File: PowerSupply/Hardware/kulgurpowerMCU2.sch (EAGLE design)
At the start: 80 parts, among them IC1 TPS77050, IC2 TPS77333DGK, X1 12Mhz, X6 C-GRID-10-70543, X7 C-GRID-10-70543, X8 C-GRID-10-70543, X9 C-GRID-10-70543

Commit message: Lot of changes to schematics. A lot.
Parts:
- removed AN3, BUZZER: TPB1,27, testpad:TPB1,27
- removed C51, C56: 0,1, SparkFun:CAP0603-CAP
- removed CN1: (no value), adafruit:USBMINIB
- removed D1, D3, D4, D5, D6: BAT54, diode:BAT54
- removed ERROR, HEARTBEAT: (no value), SparkFun:LED0603
- removed IC1: TPS77050, texas:TPS77050
- removed JP1: (no value), pinhead:PINHD-2X7
- removed R47, R52: 1k, SparkFun:RESISTOR0603-RES
- removed R50: 100k, SparkFun:RESISTOR0603-RES
- removed R51: 18k, SparkFun:RESISTOR0603-RES
- removed S3: (no value), switch-omron:10-XX
- removed S4, S5: SWITCH-MOMENTARY-212MM, SparkFun-Electromechanical:SWITCH-MOMENTARY-212MM
- removed SG2: BUZZERSMD3, SparkFun:BUZZERSMD3
- removed X6, X7, X8, X9: C-GRID-10-70543, con-molex:C-GRID-10-70543
- added AN0, EMLE, TP2, TP6, TP7: TPB1,27, testpad:TPB1,27
- added C12: 0.1, SparkFun:CAP0603-CAP
- added C14: 0,1, SparkFun:CAP0603-CAP
- added C16, C18, C41: (no value), rcl:CPOL-EUC/6032-28R
- added C19, C21, C24: 100n, rcl:C-EUC0603
- added C20, C25: 2.2nF / 50V, smd-ipc:C0402
- added C23: 1uF/ 26V, resistor:C-EUC0805
- added C27, C30, C31, C32, C33, C34, C35, C36, C37, C38, C39: 0.1, rcl:C-EUC0603
- added CN2: (no value), adafruit:USBMINIB
- added D7: BAT54, diode:BAT54
- added D8: LED-RGB-CC-THRUDIFFUSE, SparkFun-LED:LED-RGB-CC-THRUDIFFUSE
- added ERROR1, HEARTBEAT1, LED0, LED1, LED2, LED3, LED4, LED5, LED6, LED7: (no value), SparkFun:LED0603
- added IC3: REG1117-5, burr-brown:REG1117
- added JP2: (no value), pinhead:PINHD-2X7
- added L1: 4,7uH, wuerth-elektronik:WE-KIHQ_0805
- added L2, L4, L5: 4,7uH, inductors:DR73
- added R20, R21, R28, R29, R30, R31, R32, R33, R34: 1k, rcl:R-EU_R0603
- added R22: 47k, rcl:R-EU_R0603
- added R23: 100k, rcl:R-EU_R0603
- added R24, R25: 22r, rcl:R-EU_R0603
- added R26: 30k, rcl:R-EU_R0603
- added R27: 17k, rcl:R-EU_R0603
- added S6: SW1, SparkFun-Electromechanical:TAC_SWITCHSMD
- added S7: SW2, SparkFun-Electromechanical:TAC_SWITCHSMD
- added S8: SW3, SparkFun-Electromechanical:TAC_SWITCHSMD
- added S9: RESET, SparkFun-Electromechanical:SWITCH-MOMENTARY-2SIDE_EZ
- added SG1: BUZZERSMD3, SparkFun:BUZZERSMD3
- added SV2: (no value), con-lstb:MA13-2
- added TP10, TP15, TP5, TP8: TPB2,54, testpad:TPB2,54
- added TPLED0, TPLED1, TPLED2, TPLED3, TPLED4, TPLED5, TPLED6, TPLED7: LED0, testpad:TPB1,27
- added U$16, U$17, U$18, U$19: CSD97374Q4M, CSD97374Q4M:CSD97374Q4M
- added U$3: ER-OLEDM032-1, oled:ER-OLEDM032-1
- added U1, U2: MPU-6000QFN-24, SparkFun-Sensors:MPU-6000QFN-24
- C13: value 0.1 -> 0,1
- C26: value 1uF/6V -> 100n; device resistor:C-EUC0603 -> rcl:C-EUC0603
- C29: value 47uF/16V -> 0.1; device rcl:CPOL-EUC/6032-28R -> rcl:C-EUC0603
- L3: device wuerth-elektronik:WE-KIHQ_0805 -> inductors:DR73
- R10, R15, R19, R5, R6, R9: device SparkFun:RESISTOR0603-RES -> rcl:R-EU_R0603
- R12: value 30k -> 1k; device SparkFun:RESISTOR0603-RES -> rcl:R-EU_R0603
- R14: value 17k -> 1k; device SparkFun:RESISTOR0603-RES -> rcl:R-EU_R0603
- R18: value 47k -> 680k; device SparkFun:RESISTOR0603-RES -> rcl:R-EU_R0603
- R7, R8: value 22r -> 1k; device SparkFun:RESISTOR0603-RES -> rcl:R-EU_R0603
- S1: value SWS001 -> PROG; device smd-special:SWS001 -> SparkFun-Electromechanical:SWITCH-MOMENTARY-2SIDE_EZ
- S2: value SWITCH-MOMENTARY-212MM -> SW4; device SparkFun-Electromechanical:SWITCH-MOMENTARY-212MM -> SparkFun-Electromechanical:TAC_SWITCHSMD; PROD_ID (none) -> SWCH-08247
- TP1, TP3, TP4: value TPB2,54 -> TPB1,27; device testpad:TPB2,54 -> testpad:TPB1,27
- U$1: value ER-OLEDM032-1 -> EDLRD224V3R6C; device oled:ER-OLEDM032-1 -> supercap-EDLRD224V3R6C:EDLRD224V3R6C
- U$2: value EDLRD224V3R6C -> USB+SHIELD; device supercap-EDLRD224V3R6C:EDLRD224V3R6C -> SparkFun-Connectors:USB+SHIELD
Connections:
- removed net !SS1: JP1.9, U$14.!CTS1!/!RTS1!/!SS1!/SSLB0/IRQ1-DS
- removed net !SS12: U$14.PE3/D11[A11/D11]/!CTS12!/!RTS12!/!SS12!/MISOB/AN1
- removed net !SS3: JP1.5, U$14.TDO/P26/!CS6!/TXD1/!CTS3!/!RTS3!/SMOSI1/!SS3!/SSDA1/MOSIB
- removed net !SS5: U$14.PA6/A6/!CTS5!/!RTS5!/!SS5!/MOSIA
- removed net !SS9: U$14.PB4/A12/!CTS9!/!RTS9!/!SS9!
- removed net +5V: C28.1, D2.C, IC2.IN@1, IC2.IN@2
- removed net 19V: 19V.TP, R50.1
- removed net AN3: AN3.TP, C13.1, R50.2, R51.2, U$14.PE5/D13[A13/D13]/RSPCKB/IRQ5/AN3
- removed net EN_PANDA: R47.1, SG2.1
- removed net N$32: U$14.PE7/D15[A15/D15]/MISOB/IRQ7/AN5
- removed net N$33: U$14.PA0/A0/!BC0!/SSLA1
- removed net N$34: U$14.PA5/A5/RSPCKA
- removed net N$35: U$14.PA7/A7/MISOA
- removed net N$43: JP1.6
- removed net SCK0: U$14.P22/SCK0
- removed net SCK1: JP1.1, U$14.TCK/FINEC/P27/!CS7!/MTIOC2B/TMCI3/PO7/SCK1/RSPCKB
- removed net SCK12: U$14.PE0/D8[A8/D8]/SCK12/SSLB1/ANEX0
- removed net SCK3: U$14.P24/!CS4!/SCK3
- removed net SCK5: U$14.PA1/A1/SCK5/SSLA2/IRQ11
- removed net SCK6: U$14.!TRST!/P34/MTIOC0A/TMCI3/PO12/!POE2!/SCK6/SCK0/IRQ4
- removed net SCK9: U$14.PB5/A13/SCK9
- removed net SCL0: U$14.P12/RXD2/SMISO2/SSCL2/SCL0[FM+]/IRQ2
- removed net SCL5: U$14.PA3/A3/RXD5/SMISO5/SSCL5/IRQ6-DS
- removed net SDA0: U$14.P13/TXD2/SMOSI2/SSDA2/SDA0[FM+]/IRQ3/!ADTRG!
- removed net SMISO0: U$14.P21/RXD0/SMISO0/SSCL0/IRQ9
- removed net SMISO1: JP1.11, U$14.P30/RXD1/SMISO1/SSCL1/MISOB/IRQ0-DS
- removed net SMISO12: U$14.PE2/D10[A10/D10]/RXD12/SMISO12/SSCL12/RXDX12/SSLB3/MOSIB/IRQ7-DS/AN0
- removed net SMISO3: U$14.P25/!CS5!/RXD3/SMISO3/SSCL3/!ADTRG0!
- removed net SMISO5: U$14.PA2/A2/PO18/RXD5/SMISO5/SSCL5/SSLA3
- removed net SMISO6: U$14.P33/MTIOC0D/TIOCD0/TMRI3/PO11/RXD6/RXD0/SMISO6/SMISO0/SSCL6/SSCL0/IRQ3-DS
- removed net SMISO9: U$14.PB6/A14/RXD9/SMISO9/SSCL9
- removed net SMOSI0: U$14.P20/TXD0/SMOSI0/SSDA0/IRQ8
- removed net SMOSI12: U$14.PE1/D9[A9/D9]/TXD12/SMOSI12/SSDA12/TXDX12/SIOX12/SSLB2/RSPCKB/ANEX1
- removed net SMOSI3: U$14.P23/TXD3/!CTS0!/!RTS0!/SMOSI3/!SS0!/SSDA3
- removed net SMOSI5: U$14.PA4/A4/TXD5/SMOSI5/SSDA5/SSLA0/IRQ5-DS
- removed net SMOSI6: U$14.P32/TXD6/TXD0/SMOSI6/SMOSI0/SSDA6/SSDA0/IRQ3-DS
- removed net SMOSI9: U$14.PB7/A15/TXD9/SMOSI9/SSDA9
- removed net VBATT: D1.C, TP3.TP, U$14.VBATT, U$2.P
- new net !SKIP0: U$14.PA1/A1/SCK5/SSLA2/IRQ11, U$16.!SKIP
- new net !SKIP1: U$14.PA2/A2/PO18/RXD5/SMISO5/SSCL5/SSLA3, U$17.!SKIP
- new net !SKIP2: U$14.PA3/A3/RXD5/SMISO5/SSCL5/IRQ6-DS, U$18.!SKIP
- new net !SKIP3: U$14.PA5/A5/RSPCKA, U$19.!SKIP
- new net !SW1: S6.3, S6.4, U$14.P33/MTIOC0D/TIOCD0/TMRI3/PO11/RXD6/RXD0/SMISO6/SMISO0/SSCL6/SSCL0/IRQ3-DS
- new net !SW2: S7.3, S7.4, U$14.P32/TXD6/TXD0/SMOSI6/SMOSI0/SSDA6/SSDA0/IRQ3-DS
- new net !SW3!/TMS: JP2.9, S8.3, S8.4, U$14.!CTS1!/!RTS1!/!SS1!/SSLB0/IRQ1-DS
- new net !SW4!/TDI: S2.3, S2.4, U$14.P30/RXD1/SMISO1/SSCL1/MISOB/IRQ0-DS
- new net !TRST: JP2.3, U$14.!TRST!/P34/MTIOC0A/TMCI3/PO12/!POE2!/SCK6/SCK0/IRQ4
- new net +19V: 19V.TP, C30.1, C33.1, C36.1, C39.1, R23.2, SV2.14, SV2.16, U$16.VIN, U$16.VIN1, U$16.VIN2, U$16.VIN3, U$16.VIN4, U$16.VIN5, U$17.VIN, U$17.VIN1, U$17.VIN2, U$17.VIN3, U$17.VIN4, U$17.VIN5, U$18.VIN, U$18.VIN1, U$18.VIN2, U$18.VIN3, U$18.VIN4, U$18.VIN5, U$19.VIN, U$19.VIN1, U$19.VIN2, U$19.VIN3, U$19.VIN4, U$19.VIN5
- new net 5V: C16.+, C28.1, C29.1, C32.1, C35.1, C38.1, D2.C, IC2.IN@1, IC2.IN@2, IC3.VOUT, U$16.VDD, U$17.VDD, U$18.VDD, U$19.VDD
- new net AN0: AN0.TP, C12.1, R18.1, R23.1, U$14.PE2/D10[A10/D10]/RXD12/SMISO12/SSCL12/RXDX12/SSLB3/MOSIB/IRQ7-DS/AN0
- new net BAT0_EN: SV2.9, U$14.PB1/A9/TXD6/SMOSI6/SSDA6/IRQ4-DS
- new net BAT1_EN: SV2.11, U$14.PB2/A10/!CTS6!/!RTS6!/!SS6!
- new net BAT2_EN: SV2.13, U$14.PB3/A11/SCK6
- new net BAT3_EN: SV2.15, U$14.PB4/A12/!CTS9!/!RTS9!/!SS9!
- new net CPOUT1: C20.1, U1.CPOUT
- new net CPOUT2: C25.1, U2.CPOUT
- new net CS: U$14.PE4/D12[A12/D12]/SSLB0/AN2, U1.CS
- new net CS5: U$14.PC0/A16/!CTS5!/!RTS5!/!SS5!/SSLA1/IRQ14, U2.CS
- new net EN_PANDA1: R19.1, SG1.1
- new net INT_GYRO1: U$14.PE3/D11[A11/D11]/!CTS12!/!RTS12!/!SS12!/MISOB/AN1, U1.INT
- new net INT_GYRO2: U$14.PC4/A20/!CS3!/SCK5/!CTS8!/!RTS8!/!SS8!/SSLA0, U2.INT
- new net LED0: LED0.A, TPLED0.TP, U$14.P20/TXD0/SMOSI0/SSDA0/IRQ8
- new net LED1: LED1.A, TPLED1.TP, U$14.P21/RXD0/SMISO0/SSCL0/IRQ9
- new net LED2: LED2.A, TPLED2.TP, U$14.P22/SCK0
- new net LED3: LED3.A, TPLED3.TP, U$14.P23/TXD3/!CTS0!/!RTS0!/SMOSI3/!SS0!/SSDA3
- new net LED4: LED4.A, TPLED4.TP, U$14.P24/!CS4!/SCK3
- new net LED5: LED5.A, TPLED5.TP, U$14.P25/!CS5!/RXD3/SMISO3/SSCL3/!ADTRG0!
- new net LED6/TDO: JP2.5, LED6.A, TPLED6.TP, U$14.TDO/P26/!CS6!/TXD1/!CTS3!/!RTS3!/SMOSI1/!SS3!/SSDA1/MOSIB
- new net LED7/TCK: JP2.1, JP2.11, LED7.A, TPLED7.TP, U$14.TCK/FINEC/P27/!CS7!/MTIOC2B/TMCI3/PO7/SCK1/RSPCKB
- new net LED_BLUE: R34.2, U$14.P13/TXD2/SMOSI2/SSDA2/SDA0[FM+]/IRQ3/!ADTRG!
- new net LED_GREEN: R33.2, U$14.P15/RXD1/SCK3/SMISO1/SSCL1/CRX1-DS/IRQ5
- new net LED_RED: R32.2, U$14.P17/SCK1/TXD3/SMOSI3/SSDA3/MISOA/SDA2-DS/IETXD/IRQ7/!ADTRG!
- new net MISO: U$14.PE7/D15[A15/D15]/MISOB/IRQ7/AN5, U1.AD0/SDO
- new net MISO5: U$14.PC2/A18/RXD5/SMISO5/SSCL5/SSLA3/IERXD, U2.AD0/SDO
- new net MOSI: U$14.PE6/D14[A14/D14]/MOSIB/IRQ6/AN4, U1.SDA/SDI
- new net MOSI5: U$14.A19/TXD5/SMOSI5/SSDA5/IETXD, U2.SDA/SDI
- new net N$10: LED3.C, R14.2
- new net N$11: LED4.C, R28.2
- new net N$12: LED5.C, R29.2
- new net N$13: LED6.C, R30.2
- new net N$14: LED7.C, R31.2
- new net N$15: D8.GREEN_CATHODE, R33.1
- new net N$18: C37.1, U$19.BOOT
- new net N$20: C37.2, U$19.BOOT_R
- new net N$22: C27.1, U$16.BOOT
- new net N$23: C27.2, U$16.BOOT_R
- new net N$24: C34.1, U$18.BOOT
- new net N$25: C34.2, U$18.BOOT_R
- new net N$26: TP1.TP, U$14.P55/!WAIT!/CRX1/IRQ10
- new net N$28: TP3.TP, U$14.BCLK/P53
- new net N$30: TP6.TP, U$14.PA7/A7/MISOA
- new net N$7: ERROR1.C, R21.2
- new net OUT1_EN: SV2.18, U$14.PB5/A13/SCK9
- new net OUT2_EN: SV2.20, U$14.PB6/A14/RXD9/SMISO9/SSCL9
- new net OUT3_EN: SV2.22, U$14.PB7/A15/TXD9/SMOSI9/SSDA9
- new net OUT4_EN: SV2.24, U$14.PE0/D8[A8/D8]/SCK12/SSLB1/ANEX0
- new net OUT5_EN: SV2.26, U$14.PE1/D9[A9/D9]/TXD12/SMOSI12/SSDA12/TXDX12/SIOX12/SSLB2/RSPCKB/ANEX1
- new net PWM0: U$14.PA0/A0/!BC0!/SSLA1, U$16.PWM
- new net PWM1: U$14.PA4/A4/TXD5/SMOSI5/SSDA5/SSLA0/IRQ5-DS, U$17.PWM
- new net PWM2: U$14.PA6/A6/!CTS5!/!RTS5!/!SS5!/MOSIA, U$18.PWM
- new net PWM3: U$14.PB0/A8/RXD6/SMISO6/SSCL6/RSPCKA/IRQ12, U$19.PWM
- new net REGOUT1: C19.1, U1.REGOUT
- new net REGOUT2: C24.1, U2.REGOUT
- new net SCLK: U$14.PE5/D13[A13/D13]/RSPCKB/IRQ5/AN3, U1.SCL/SCLK
- new net SCLK5: U$14.PC1/A17/SCK5/SSLA2/IRQ12, U2.SCL/SCLK
- new net SUPERCAP: D7.C, U$1.P, U$14.VBATT
- new net USB0_VBUS: R26.1, R27.2, U$14.P16/TXD1/RXD3/SMOSI1/SMISO3/SSDA1/SSCL3/MOSIA/SCL2-DS/IERXD/USB0_VBUS/IRQ6/!ADTRG0!
- new net V+: C23.1, C41.+, IC3.VIN, SV2.12
- new net VSW0: L2.1, TP8.TP, U$16.VSW, U$16.VSW1, U$16.VSW2, U$16.VSW3, U$16.VSW4, U$16.VSW5
- new net VSW1: L3.1, TP5.TP, U$17.VSW, U$17.VSW1, U$17.VSW2, U$17.VSW3, U$17.VSW4, U$17.VSW5
- new net VSW2: L4.1, TP10.TP, U$18.VSW, U$18.VSW1, U$18.VSW2, U$18.VSW3, U$18.VSW4, U$18.VSW5
- new net VSW3: L5.1, TP15.TP, U$19.VSW, U$19.VSW1, U$19.VSW2, U$19.VSW3, U$19.VSW4, U$19.VSW5
- net !OLED_CS: now also JP2.10, U$3.!CS; no longer JP1.10, U$1.!CS
- net !OLED_DC: now also U$3.!DC; no longer U$1.!DC
- net !OLED_RD: now also U$3.!RD; no longer U$1.!RD
- net !OLED_RESET: now also U$3.!RESET; no longer U$1.!RESET
- net !OLED_WR: now also U$3.!WR; no longer U$1.!WR
- net !RESET: now also JP2.13, R22.2, S9.1; no longer JP1.13, R18.2, S3.P, S3.P1
- net +3V3: now also C14.1, C18.+, C21.1, D7.A, JP2.8, L1.2, R22.1, U$3.VBAT, U1.VDD, U2.VDD; no longer C29.+, C56.1, D1.A, JP1.8, L3.2, R18.1, U$1.VBAT
- net AVCC0: now also C13.1, L1.1; no longer C51.1, L3.1
- net BUZZER: now also R19.2, U$14.P05/IRQ13/DA1; no longer BUZZER.TP, R47.2
- net D+: now also CN2.D+, R25.2, U$2.D+; no longer CN1.D+, R8.2
- net D-: now also CN2.D-, R24.2, U$2.D-; no longer CN1.D-, R7.2
- net D0: now also U$3.DB0; no longer U$1.DB0
- net D1: now also U$3.DB1; no longer U$1.DB1
- net D2: now also U$3.DB2; no longer U$1.DB2
- net D3: now also U$3.DB3; no longer U$1.DB3
- net D4: now also U$3.DB4; no longer U$1.DB4
- net D5: now also U$3.DB5; no longer U$1.DB5
- net D6: now also U$3.DB6; no longer U$1.DB6
- net D7: now also U$3.DB7; no longer U$1.DB7
- net EMLE: now also EMLE.TP, JP2.4; no longer JP1.4, TP1.TP
- net ERROR: now also ERROR1.A; no longer ERROR.A
- net GND: now also C12.2, C14.2, C16.-, C18.-, C19.2, C20.2, C21.2, C23.2, C24.2, C25.2, C29.2, C30.2, C32.2, C33.2, C35.2, C36.2, C38.2, C39.2, C41.-, CN2.GND, D8.CATHODE, IC3.GND, JP2.12, JP2.14, JP2.2, R12.1, R14.1, R18.2, R20.1, R21.1, R26.2, R28.1, R29.1, R30.1, R31.1, R7.1, R8.1, S1.2, S2.1, S2.2, S6.1, S6.2, S7.1, S7.2, S8.1, S8.2, S9.2, SG1.2, SV2.10, SV2.17, U$1.N, U$16.GND, U$16.PAD, U$17.GND, U$17.PAD, U$18.GND, U$18.PAD, U$19.GND, U$19.PAD, U$2.GND, U$2.P$1, U$2.P$2, U$3.VSS, U1.CLKIN, U1.GND, U2.CLKIN, U2.GND; no longer C29.-, C51.2, C56.2, CN1.GND, IC1.GND, JP1.12, JP1.14, JP1.2, R12.2, R19.1, R51.1, R52.1, S1.1, S3.S, S3.S1, SG2.2, U$1.VSS, U$2.N, X6-3.S, X7-3.S, X8-3.S, X9-3.S
- net HEARTBEAT: now also HEARTBEAT1.A, U$14.P12/RXD2/SMISO2/SSCL2/SCL0[FM+]/IRQ2; no longer HEARTBEAT.A, U$14.P05/IRQ13/DA1
- net IBAT0_AD: now also SV2.19; no longer X6-2.S
- net IBAT1_AD: now also SV2.21; no longer X7-2.S
- net IBAT2_AD: now also SV2.23; no longer X8-2.S
- net IBAT3_AD: now also SV2.25; no longer X9-2.S
- net MD: now also JP2.7, S1.1; no longer JP1.7, S1.2, TP4.TP
- net N$17: now also D8.BLUE_CATHODE, R34.1; no longer HEARTBEAT.C, R19.2
- net N$19: now also C31.1, U$17.BOOT; no longer U$14.P15/RXD1/SCK3/SMISO1/SSCL1/CRX1-DS/IRQ5
- net N$2: now also LED0.C, R7.2; no longer R12.1, R14.2, U$14.P16/TXD1/RXD3/SMOSI1/SMISO3/SSDA1/SSCL3/MOSIA/SCL2-DS/IERXD/USB0_VBUS/IRQ6/!ADTRG0!
- net N$21: now also C31.2, U$17.BOOT_R; no longer U$14.PJ3/MTIOC3C/!CTS6!/!RTS6!/!CTS0!/!RTS0!/!SS6!/!SS0!
- net N$27: now also TP2.TP, U$14.P54/ALE/!CTS2!/!RTS2!/!SS2!/CTX1; no longer U$14.PE4/D12[A12/D12]/SSLB0/AN2
- net N$29: now also TP4.TP, U$14.PJ3/MTIOC3C/!CTS6!/!RTS6!/!CTS0!/!RTS0!/!SS6!/!SS0!; no longer ERROR.C, R52.2
- net N$31: now also TP7.TP, U$14.PC5/A21/!CS2!/!WAIT!/SCK8/RSPCKA; no longer U$14.PE6/D14[A14/D14]/MOSIB/IRQ6/AN4
- net N$4: now also D8.RED_CATHODE, R32.1; no longer D3.C, D4.C, D5.C, D6.C, IC1.IN
- net N$5: now also HEARTBEAT1.C, R20.2; no longer IC1.!EN
- net N$8: now also LED1.C, R8.2; no longer IC1.OUT
- net N$9: now also LED2.C, R12.2; no longer IC1.NC/FB
- net USB0_DM: now also R24.1; no longer R7.1
- net USB0_DP: now also R25.1; no longer R8.1
- net VBAT0: now also L2.2, SV2.1, SV2.2; no longer D3.A, X6-1.S
- net VBAT1: now also L3.2, SV2.3, SV2.4; no longer D4.A, X7-1.S
- net VBAT2: now also L4.2, SV2.5, SV2.6; no longer D5.A, X8-1.S
- net VBAT3: now also L5.2, SV2.7, SV2.8; no longer D6.A, X9-1.S
- net VBUS: now also CN2.VBUS, R27.1, U$2.VBUS; no longer CN1.VBUS, R14.1
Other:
- note added: "12MHz main crystal"
- note added: "3.3V"
- note added: "3.3V, 250mA"
- note added: "32kHz timer crystal"
- note added: "5V total max current on this sheet 33mA"
- note added: "5V, 500mA"
- note added: "Analog VCC filter"
- note added: "Board to board connector, AD dividers"
- note added: "Buttons"
- note added: "Buzzer"
- note added: "Gyroscopes"
- note added: "LEDs"
- note added: "LIPO chargers"
- note added: "OLED"
- note added: "Power supplies"
- note added: "RTC backup supply"
- note added: "USB"
- note added: "User interface"
- note removed: "118/18*3.3=21.633"
- note removed: "Farnell 1192551"
- note removed: "LiPo batteries, positive inputs"

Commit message: lot of work done on schematics
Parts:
- removed SV2: (no value), con-lstb:MA13-2
- removed TP6, TP7: TPB1,27, testpad:TPB1,27
- added X2: 2534-, con-3m:2534-
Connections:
- removed net N$30: TP6.TP, U$14.PA7/A7/MISOA
- removed net N$31: TP7.TP, U$14.PC5/A21/!CS2!/!WAIT!/SCK8/RSPCKA
- new net COMPUTER_PWR: U$14.PC5/A21/!CS2!/!WAIT!/SCK8/RSPCKA, X2-28.KL
- new net ENABLE_PWR: U$14.PA7/A7/MISOA, X2-30.KL
- new net IMON1: X2-27.KL
- new net IMON2: X2-29.KL
- new net PGOOD1: X2-31.KL
- new net PGOOD2: X2-33.KL
- new net PWM_A: X2-34.KL
- new net PWM_B: X2-32.KL
- net +19V: now also X2-14.KL, X2-16.KL; no longer SV2.14, SV2.16
- net BAT0_EN: now also X2-9.KL; no longer SV2.9
- net BAT1_EN: now also X2-11.KL; no longer SV2.11
- net BAT2_EN: now also X2-13.KL; no longer SV2.13
- net BAT3_EN: now also X2-15.KL; no longer SV2.15
- net GND: now also X2-10.KL, X2-17.KL; no longer SV2.10, SV2.17
- net IBAT0_AD: now also X2-19.KL; no longer SV2.19
- net IBAT1_AD: now also X2-21.KL; no longer SV2.21
- net IBAT2_AD: now also X2-23.KL; no longer SV2.23
- net IBAT3_AD: now also X2-25.KL; no longer SV2.25
- net OUT1_EN: now also X2-18.KL; no longer SV2.18
- net OUT2_EN: now also X2-20.KL; no longer SV2.20
- net OUT3_EN: now also X2-22.KL; no longer SV2.22
- net OUT4_EN: now also X2-24.KL; no longer SV2.24
- net OUT5_EN: now also X2-26.KL; no longer SV2.26
- net V+: now also X2-12.KL; no longer SV2.12
- net VBAT0: now also X2-1.KL, X2-2.KL; no longer SV2.1, SV2.2
- net VBAT1: now also X2-3.KL, X2-4.KL; no longer SV2.3, SV2.4
- net VBAT2: now also X2-5.KL, X2-6.KL; no longer SV2.5, SV2.6
- net VBAT3: now also X2-7.KL, X2-8.KL; no longer SV2.7, SV2.8
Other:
- moved on the sheet: 19V, AN0, C1, C12, C15, C2, C8, R1, R11, R13, R16, R17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

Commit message: More work on electronics
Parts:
- removed ERROR1, HEARTBEAT1: (no value), SparkFun:LED0603
- removed R20, R21: 1k, rcl:R-EU_R0603
- removed TP1, TP2, TP3, TP4: TPB1,27, testpad:TPB1,27
- added C22, C40: 0.1, rcl:C-EUC0603
- added C42, C43, C44, C45: (no value), rcl:CPOL-EUC/6032-28R
- added C46, C47, C48, C49: 0,1, SparkFun:CAP0603-CAP
- added R35, R36: 10k, rcl:R-EU_R0603
- added X3: 22-23-2021, con-molex:22-23-2021
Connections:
- net CS renamed SSLB0
- net MISO renamed MISOB
- net MOSI renamed MOSIB
- net N$1 renamed USB0_DPUPE
- removed net CS5: U$14.PC0/A16/!CTS5!/!RTS5!/!SS5!/SSLA1/IRQ14, U2.CS
- removed net ERROR: ERROR1.A, U$14.P07/IRQ15/!ADTRG0
- removed net HEARTBEAT: HEARTBEAT1.A, U$14.P12/RXD2/SMISO2/SSCL2/SCL0[FM+]/IRQ2
- removed net MISO5: U$14.PC2/A18/RXD5/SMISO5/SSCL5/SSLA3/IERXD, U2.AD0/SDO
- removed net MOSI5: U$14.A19/TXD5/SMOSI5/SSDA5/IETXD, U2.SDA/SDI
- removed net N$26: TP1.TP, U$14.P55/!WAIT!/CRX1/IRQ10
- removed net N$27: TP2.TP, U$14.P54/ALE/!CTS2!/!RTS2!/!SS2!/CTX1
- removed net N$28: TP3.TP, U$14.BCLK/P53
- removed net N$29: TP4.TP, U$14.PJ3/MTIOC3C/!CTS6!/!RTS6!/!CTS0!/!RTS0!/!SS6!/!SS0!
- removed net N$5: HEARTBEAT1.C, R20.2
- removed net N$7: ERROR1.C, R21.2
- removed net PWM_A: X2-34.KL
- removed net PWM_B: X2-32.KL
- removed net SCLK: U$14.PE5/D13[A13/D13]/RSPCKB/IRQ5/AN3, U1.SCL/SCLK
- removed net SCLK5: U$14.PC1/A17/SCK5/SSLA2/IRQ12, U2.SCL/SCLK
- new net AN1: C22.1, R35.2, U$14.PE3/D11[A11/D11]/!CTS12!/!RTS12!/!SS12!/MISOB/AN1
- new net AN3: C40.1, R36.2, U$14.PE5/D13[A13/D13]/RSPCKB/IRQ5/AN3
- new net MISOA: R9.2, U$14.PC7/A23/!CS0!/TXD8/SMOSI8/SSDA8/MISOA/IRQ14, U2.AD0/SDO
- new net MOSIA: U$14.PC6/A22/!CS1!/RXD8/SMISO8/SSCL8/MOSIA/IRQ13, U2.SDA/SDI
- new net PWM4: U$14.PB4/A12/!CTS9!/!RTS9!/!SS9!, X2-34.KL
- new net PWM5: U$14.PB6/A14/RXD9/SMISO9/SSCL9, X2-32.KL
- new net RSPCKA: U$14.PC5/A21/!CS2!/!WAIT!/SCK8/RSPCKA, U2.SCL/SCLK
- new net RSPCKB: U$14.PE1/D9[A9/D9]/TXD12/SMOSI12/SSDA12/TXDX12/SIOX12/SSLB2/RSPCKB/ANEX1, U1.SCL/SCLK
- new net SSLA0: U$14.PC4/A20/!CS3!/SCK5/!CTS8!/!RTS8!/!SS8!/SSLA0, U2.CS
- net !OLED_CS: now also U$14.P55/!WAIT!/CRX1/IRQ10; no longer U$14.PC6/A22/!CS1!/RXD8/SMISO8/SSCL8/MOSIA/IRQ13
- net !OLED_DC: now also U$14.P54/ALE/!CTS2!/!RTS2!/!SS2!/CTX1; no longer R9.2, U$14.PC7/A23/!CS0!/TXD8/SMOSI8/SSDA8/MISOA/IRQ14
- net !TRST: now also X3-1.S
- net +3V3: now also C46.1, C47.1, C48.1, C49.1
- net BAT0_EN: now also U$14.PA7/A7/MISOA; no longer U$14.PB1/A9/TXD6/SMOSI6/SSDA6/IRQ4-DS
- net BAT1_EN: now also U$14.PB1/A9/TXD6/SMOSI6/SSDA6/IRQ4-DS; no longer U$14.PB2/A10/!CTS6!/!RTS6!/!SS6!
- net BAT2_EN: now also U$14.PB2/A10/!CTS6!/!RTS6!/!SS6!; no longer U$14.PB3/A11/SCK6
- net BAT3_EN: now also U$14.PB3/A11/SCK6; no longer U$14.PB4/A12/!CTS9!/!RTS9!/!SS9!
- net COMPUTER_PWR: now also U$14.PE0/D8[A8/D8]/SCK12/SSLB1/ANEX0; no longer U$14.PC5/A21/!CS2!/!WAIT!/SCK8/RSPCKA
- net ENABLE_PWR: now also U$14.P12/RXD2/SMISO2/SSCL2/SCL0[FM+]/IRQ2; no longer U$14.PA7/A7/MISOA
- net GND: now also C22.2, C40.2, C42.-, C43.-, C44.-, C45.-, C46.2, C47.2, C48.2, C49.2, X3-2.S; no longer R20.1, R21.1
- net IMON1: now also R35.1
- net IMON2: now also R36.1
- net INT_GYRO1: now also U$14.PC1/A17/SCK5/SSLA2/IRQ12; no longer U$14.PE3/D11[A11/D11]/!CTS12!/!RTS12!/!SS12!/MISOB/AN1
- net INT_GYRO2: now also U$14.PC0/A16/!CTS5!/!RTS5!/!SS5!/SSLA1/IRQ14; no longer U$14.PC4/A20/!CS3!/SCK5/!CTS8!/!RTS8!/!SS8!/SSLA0
- net OUT2_EN: now also U$14.PB7/A15/TXD9/SMOSI9/SSDA9; no longer U$14.PB6/A14/RXD9/SMISO9/SSCL9
- net OUT3_EN: now also U$14.PJ3/MTIOC3C/!CTS6!/!RTS6!/!CTS0!/!RTS0!/!SS6!/!SS0!; no longer U$14.PB7/A15/TXD9/SMOSI9/SSDA9
- net OUT4_EN: now also U$14.BCLK/P53; no longer U$14.PE0/D8[A8/D8]/SCK12/SSLB1/ANEX0
- net OUT5_EN: now also U$14.P07/IRQ15/!ADTRG0; no longer U$14.PE1/D9[A9/D9]/TXD12/SMOSI12/SSDA12/TXDX12/SIOX12/SSLB2/RSPCKB/ANEX1
- net PGOOD1: now also U$14.A19/TXD5/SMOSI5/SSDA5/IETXD
- net PGOOD2: now also U$14.PC2/A18/RXD5/SMISO5/SSCL5/SSLA3/IERXD
- net VBAT0: now also C42.+
- net VBAT1: now also C43.+
- net VBAT2: now also C44.+
- net VBAT3: now also C45.+
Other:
- moved on the sheet: C1, C15, C2, C29, C30, C32, C33, C35, C36, C38, C39, C8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

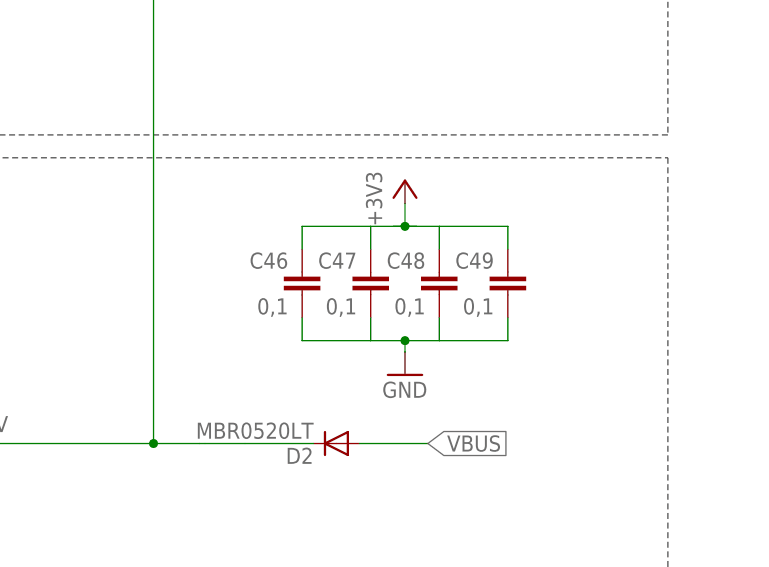
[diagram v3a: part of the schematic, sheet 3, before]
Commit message: Converted into 2 layer board from 4 layer. Seems to be OK for production
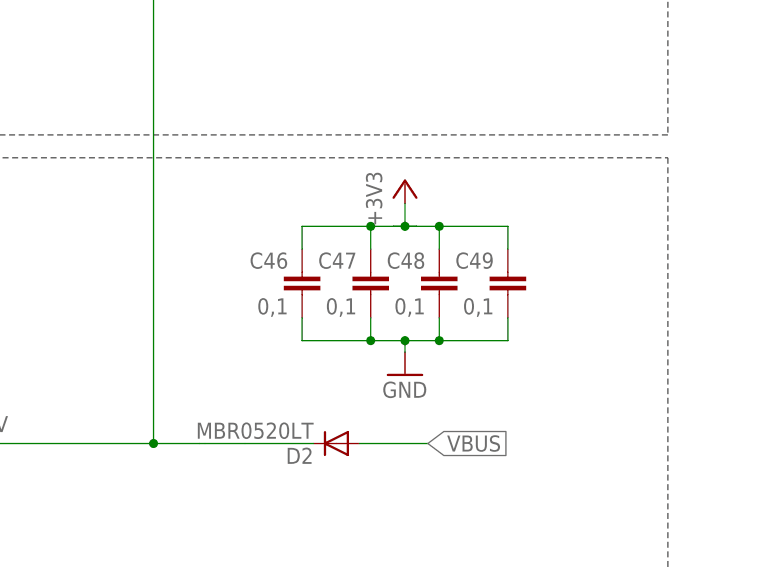
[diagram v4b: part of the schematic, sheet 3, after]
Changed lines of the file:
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@@
 <wire x1="115.57" y1="82.55" x2="115.57" y2="83.82" width="0.1524" layer="91"/>
 <junction x="115.57" y="83.82"/>
+<junction x="119.38" y="83.82"/>
+<junction x="111.76" y="83.82"/>
 </segment>
 </net>
@@
 <wire x1="115.57" y1="96.52" x2="115.57" y2="99.06" width="0.1524" layer="91"/>
 <junction x="115.57" y="96.52"/>
+<junction x="111.76" y="96.52"/>
+<junction x="119.38" y="96.52"/>
 </segment>
 </net>

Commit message: Minor bugfixes to boards.
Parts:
- added D1: MBRS320T3, diode:MBRS320T3
- D8: value LED-RGB-CC-THRUDIFFUSE -> WP154A4SUREQBFZGW
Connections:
- net EN_PANDA1 renamed BUZZER_X
- new net VIN: C30.1, C33.1, C36.1, C39.1, D1.C, U$16.VIN, U$16.VIN1, U$16.VIN2, U$16.VIN3, U$16.VIN4, U$16.VIN5, U$17.VIN, U$17.VIN1, U$17.VIN2, U$17.VIN3, U$17.VIN4, U$17.VIN5, U$18.VIN, U$18.VIN1, U$18.VIN2, U$18.VIN3, U$18.VIN4, U$18.VIN5, U$19.VIN, U$19.VIN1, U$19.VIN2, U$19.VIN3, U$19.VIN4, U$19.VIN5
- net +19V: now also D1.A; no longer C30.1, C33.1, C36.1, C39.1, U$16.VIN, U$16.VIN1, U$16.VIN2, U$16.VIN3, U$16.VIN4, U$16.VIN5, U$17.VIN, U$17.VIN1, U$17.VIN2, U$17.VIN3, U$17.VIN4, U$17.VIN5, U$18.VIN, U$18.VIN1, U$18.VIN2, U$18.VIN3, U$18.VIN4, U$18.VIN5, U$19.VIN, U$19.VIN1, U$19.VIN2, U$19.VIN3, U$19.VIN4, U$19.VIN5
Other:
- moved on the sheet: C30, C33, C36, C39, U2

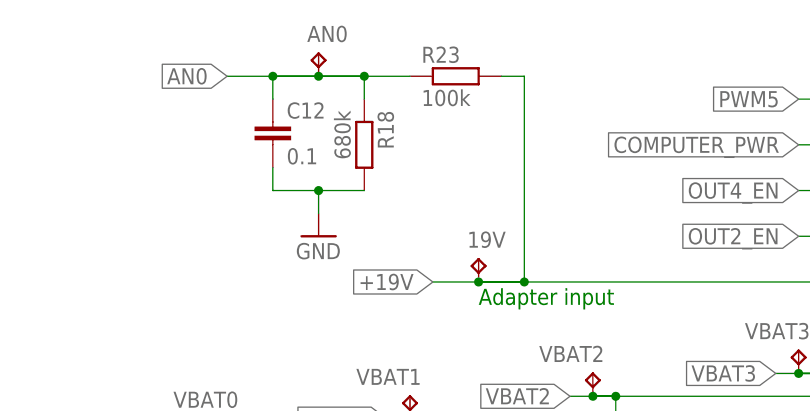
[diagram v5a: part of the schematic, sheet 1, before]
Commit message: Two resistors in ladder were swapped Nominals rised for pullup. Next power bill will be smaller!
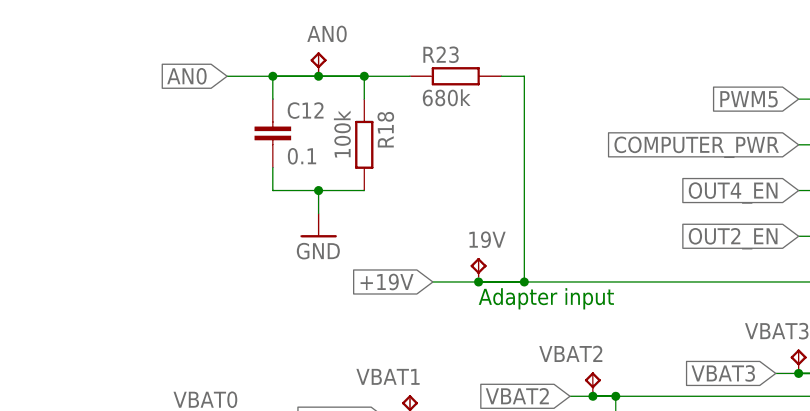
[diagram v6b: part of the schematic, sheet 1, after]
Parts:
- R18: value 680k -> 100k
- R23: value 100k -> 680k
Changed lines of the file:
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@@
 <attribute name="TP_SIGNAL_NAME" value=""/>
 </part>
-<part name="R18" library="rcl" deviceset="R-EU_" device="R0603" value="680k"/>
-<part name="R23" library="rcl" deviceset="R-EU_" device="R0603" value="100k"/>
+<part name="R18" library="rcl" deviceset="R-EU_" device="R0603" value="100k"/>
+<part name="R23" library="rcl" deviceset="R-EU_" device="R0603" value="680k"/>
 <part name="R24" library="rcl" deviceset="R-EU_" device="R0603" value="22r"/>
 <part name="R25" library="rcl" deviceset="R-EU_" device="R0603" value="22r"/>
